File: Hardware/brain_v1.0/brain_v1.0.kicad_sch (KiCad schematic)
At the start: 50 parts, among them J1 UART, J2 Conn_01x02, J3 Conn_01x02, J4 Conn_01x02, J5 JTAG, J6 Conn_01x02, J9 UART Backup, Q1 BSS138, Q2 BSS138, Q3 BSS138, Q4 BSS138, Q5 SMD-TRANSISTORS-NPN-25V-500MW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, Q6 SMD-TRANSISTORS-NPN-25V-500MW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, SW1 SW_Push, SW3 SW_Push, U1 ESP32-WROOM-32E 4MB

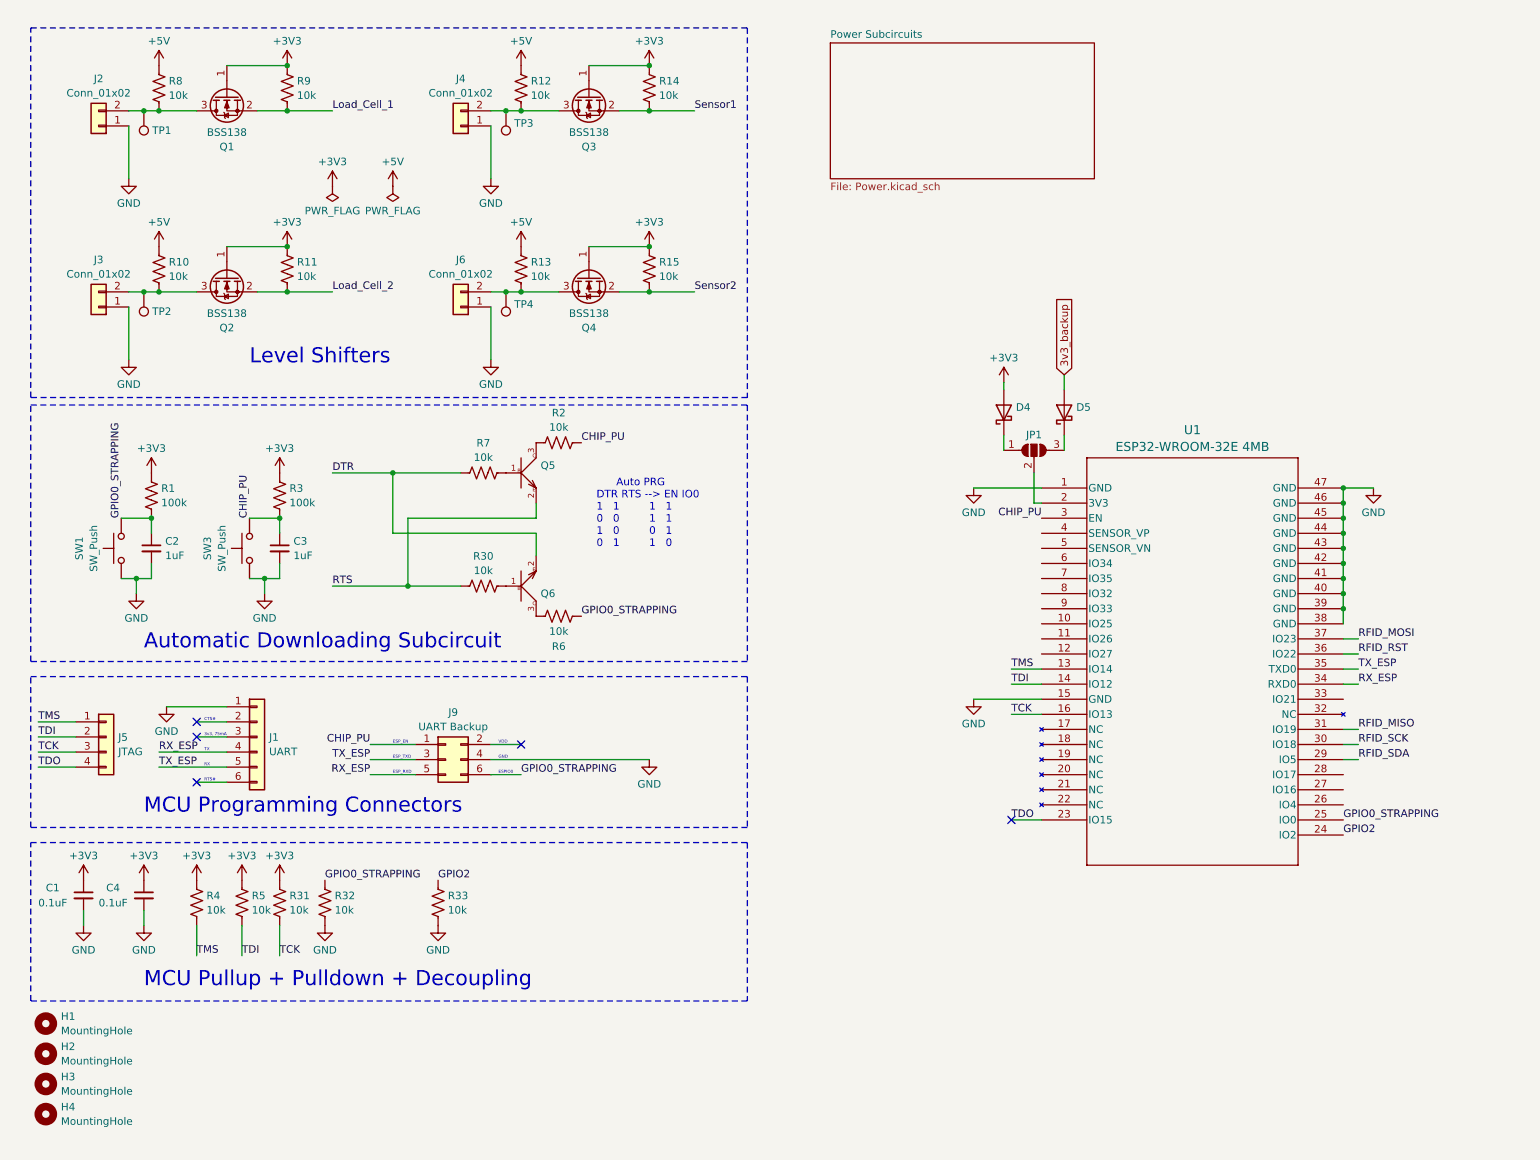
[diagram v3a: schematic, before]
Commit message: everything done on design and parts for first board run except for ADC; onto layout
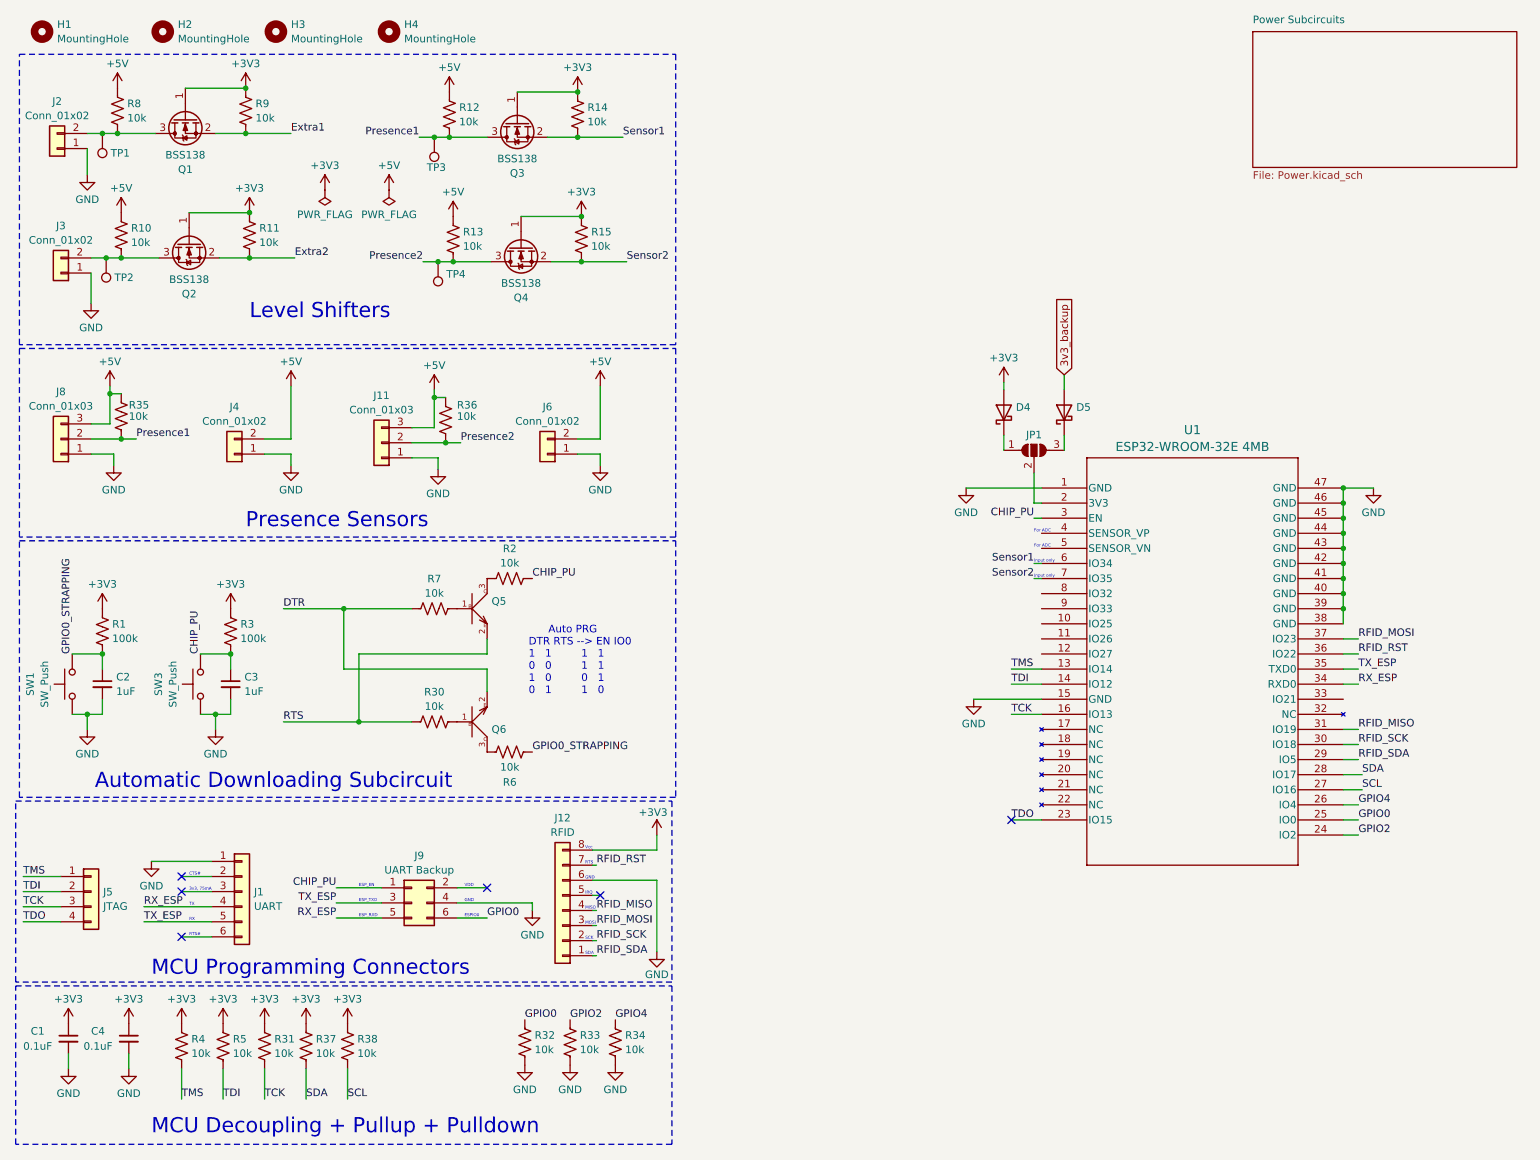
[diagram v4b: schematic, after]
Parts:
- added J11, J8: Conn_01x03, Connector_Molex:Molex_KK-254_AE-6410-03A_1x03_P2.54mm_Vertical, symbol Connector_Generic:Conn_01x03
- added J12: RFID, Connector_Harting:Harting_har-flexicon_14110813001xxx_1x08-MP_P2.54mm_Vertical, symbol Connector_Generic:Conn_01x08
- added R34, R35, R36, R37, R38: 10k, Resistor_SMD:R_1206_3216Metric, symbol Device:R_US
- J1: footprint (none) -> Connector_PinHeader_2.54mm:PinHeader_1x06_P2.54mm_Vertical; Link (none) -> https://www.digikey.com/en/products/detail/harwin-inc/M20-9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; MPN (none) -> M20-9990645
- J5: footprint (none) -> Connector_PinSocket_2.54mm:PinSocket_1x04_P2.54mm_Vertical; Link (none) -> https://www.digikey.com/en/products/detail/harwin-inc/M20-9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; MPN (none) -> M20-9990446
- J9: footprint (none) -> 61200621621:61200621621; Link (none) -> https://www.digikey.com/en/products/detail/w%C3%BCrth-elekt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; MPN (none) -> 61200621621
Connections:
- net +3V3: now also J12.8 (Pin_8), R37.1, R38.1
- net +5V: now also J4.2 (Pin_2), J6.2 (Pin_2), J11.3 (Pin_3), J8.3 (Pin_3), R35.1, R36.1
- net GND: now also J11.1 (Pin_1), J12.6 (Pin_6), J8.1 (Pin_1), R34.2
- net GPIO0_STRAPPING: no longer J9.6 (Pin_6), R32.1, U1.25 (IO0)
- net RFID_MISO: now also J12.4 (Pin_4)
- net RFID_MOSI: now also J12.3 (Pin_3)
- net RFID_RST: now also J12.7 (Pin_7)
- net RFID_SCK: now also J12.2 (Pin_2)
- net RFID_SDA: now also J12.1 (Pin_1)
- net Sensor1: now also U1.6 (IO34)
- net Sensor2: now also U1.7 (IO35)
- net Presence2: now reaches Q4.3 (D), R13.2, TP4.1
- net Presence2: now also J11.2 (Pin_2), R36.2; no longer J6.2 (Pin_2)
- net Presence1: now reaches Q3.3 (D), R12.2, TP3.1
- net Presence1: now also J8.2 (Pin_2), R35.2; no longer J4.2 (Pin_2)
- net GPIO4: now reaches U1.26 (IO4)
- net GPIO4: now also R34.1
- net SCL: now reaches U1.27 (IO16)
- net SCL: now also R38.2
- net SDA: now reaches U1.28 (IO17)
- net SDA: now also R37.2
- net Load_Cell_1 renamed Extra1
- net Load_Cell_2 renamed Extra2
- new net GPIO0: J9.6 (Pin_6), R32.1, U1.25 (IO0)
- no-connect marks 5 -> 6
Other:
- note added: "For ADC"
- note added: "IRQ"
- note added: "Input only"
- note added: "MCU Decoupling + Pullup + Pulldown"
- note added: "MISO"
- note added: "MOSI"
- note added: "Presence Sensors"
- note added: "RTS"
- note added: "SCK"
- note added: "SDA"
- note added: "Vcc"
- note removed: "MCU Pullup + Pulldown + Decoupling"
- moved on the sheet: C1, C2, C3, C4, H1, H2, H3, H4, J1, J2, J3, J4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

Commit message: finished part selection and schematic for brain. Created RFID and Motor Driver boards
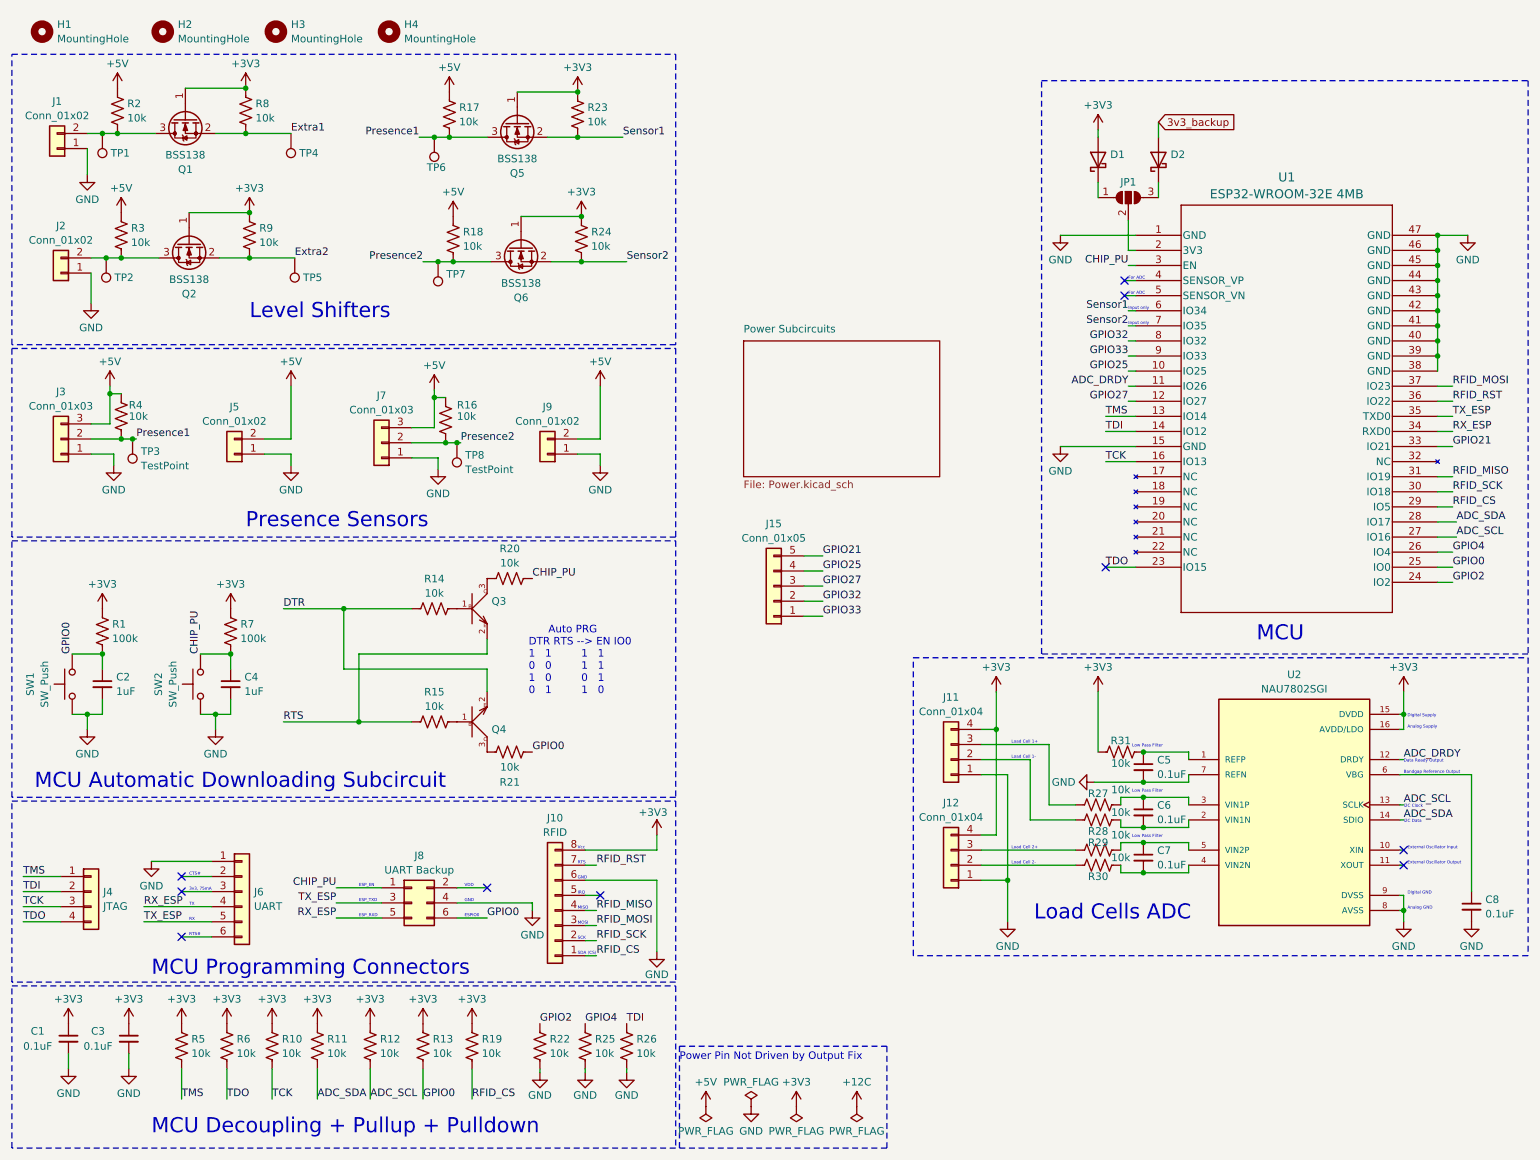
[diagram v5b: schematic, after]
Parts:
- removed R34: 10k, Resistor_SMD:R_1206_3216Metric, symbol Device:R_US
- added C5, C6, C7, C8: 0.1uF, Capacitor_SMD:C_0603_1608Metric, symbol Device:C_Small
- added J11, J12: Conn_01x04, Connector_Molex:Molex_KK-254_AE-6410-04A_1x04_P2.54mm_Vertical, symbol Connector_Generic:Conn_01x04
- added J15: Conn_01x05, symbol Connector_Generic:Conn_01x05
- added R13, R19, R26, R27, R28, R29, R30, R31: 10k, Resistor_SMD:R_1206_3216Metric, symbol Device:R_US
- added TP3, TP4, TP5, TP8: TestPoint, TestPoint:TestPoint_Keystone_5010-5014_Multipurpose, symbol Connector:TestPoint
- added U2: NAU7802SGI, NAU7802SGI:SOIC127P600X175-16N, symbol NAU7802SGI:NAU7802SGI
- renumbered C4 to C3, C3 to C4, D4 to D1, D5 to D2, J2 to J1, J12 to J10, J3 to J2, J8 to J3, J5 to J4, J4 to J5, J1 to J6, J11 to J7, J9 to J8, J6 to J9, Q5 to Q3, Q6 to Q4, Q3 to Q5, Q4 to Q6, R31 to R10, R37 to R11, R38 to R12, R7 to R14, R30 to R15, R36 to R16, R12 to R17, R13 to R18, R8 to R2, R2 to R20, R6 to R21, R32 to R22, R14 to R23, R15 to R24, R33 to R25, R10 to R3, R35 to R4, R4 to R5, R5 to R6, R3 to R7, R9 to R8, R11 to R9, SW3 to SW2, TP3 to TP6, TP4 to TP7
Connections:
- net GPIO0_STRAPPING is gone; now on net GPIO0: C2.1, R1.2, R21.2, SW1.2
- net +3V3: now also J11.4 (Pin_4), J12.4 (Pin_4), R13.1, R19.1, R31.1, U2.15 (DVDD), U2.16 (AVDD/LDO)
- net Extra1: now also TP4.1
- net Extra2: now also TP5.1
- net GND: now also C5.2, C8.2, J11.1 (Pin_1), J12.1 (Pin_1), R26.2, U2.7 (REFN), U2.8 (AVSS), U2.9 (DVSS)
- net GPIO0: now also R13.2; no longer R22.1
- net GPIO2: now also R22.1; no longer R25.1
- net GPIO4: now also R25.1
- net Presence1: now also TP3.1
- net Presence2: now also TP8.1
- net TDI: now also R26.1; no longer R6.2
- net TDO: now also R6.2
- net GPIO25: now reaches U1.10 (IO25)
- net GPIO25: now also J15.4 (Pin_4)
- net ADC_DRDY: now reaches U1.11 (IO26)
- net ADC_DRDY: now also U2.12 (DRDY)
- net GPIO27: now reaches U1.12 (IO27)
- net GPIO27: now also J15.3 (Pin_3)
- net GPIO21: now reaches U1.33 (IO21)
- net GPIO21: now also J15.5 (Pin_5)
- net GPIO32: now reaches U1.8 (IO32)
- net GPIO32: now also J15.2 (Pin_2)
- net GPIO33: now reaches U1.9 (IO33)
- net GPIO33: now also J15.1 (Pin_1)
- net RFID_SDA renamed RFID_CS
- net RFID_CS: now also R19.2
- net SCL renamed ADC_SCL
- net ADC_SCL: now also U2.13 (SCLK)
- net SDA renamed ADC_SDA
- net ADC_SDA: now also U2.14 (SDIO)
- new net: C5.1, R31.2, U2.1 (REFP)
- new net: C6.1, R27.2, U2.3 (VIN1P)
- new net: C6.2, R28.2, U2.2 (VIN1N)
- new net: C7.1, R29.2, U2.5 (VIN2P)
- new net: C7.2, R30.2, U2.4 (VIN2N)
- new net: C8.1, U2.6 (VBG)
- new net: J12.2 (Pin_2), R30.1
- new net: J11.2 (Pin_2), R28.1
- new net: J11.3 (Pin_3), R27.1
- new net: J12.3 (Pin_3), R29.1
- no-connect marks 6 -> 10
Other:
- note added: "Analog GND"
- note added: "Analog Supply"
- note added: "Bandgap Reference Output"
- note added: "Data Ready Output"
- note added: "Digital GND"
- note added: "Digital Supply"
- note added: "External Oscillator Input"
- note added: "External Oscillator Output"
- note added: "I2C Clock"
- note added: "I2C Data"
- note added: "Load Cell 1+"
- note added: "Load Cell 1-"
- note added: "Load Cell 2+"
- note added: "Load Cell 2-"
- note added: "Load Cells ADC"
- note added: "Low Pass Filter"
- note added: "MCU"
- note added: "MCU Automatic Downloading Subcircuit"
- note added: "Power Pin Not Driven by Output Fix"
- note added: "SDA (CS)"
- note removed: "Automatic Downloading Subcircuit"
- note removed: "SDA"
- moved on the sheet: D1, D2, J10, JP1, R10, R11, R12, R22, R25, R6, U1

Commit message: RFID board schematic done, antenna head created in the layout
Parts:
- J15: footprint (none) -> Connector_PinHeader_2.54mm:PinHeader_1x05_P2.54mm_Vertical; Link (none) -> https://www.digikey.com/en/products/detail/harwin-inc/M20-9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; MPN (none) -> M20-9990546
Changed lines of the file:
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@@
       (effects (font (size 1.27 1.27)))
     )
-    (property "Footprint" "" (at 140.335 109.22 0)
+    (property "Footprint" "Connector_PinHeader_2.54mm:PinHeader_1x05_P2.54mm_Vertical" (at 140.335 109.22 0)
       (effects (font (size 1.27 1.27)) hide)
     )
@@
       (effects (font (size 1.27 1.27)) hide)
     )
+    (property "Link" "https://www.digikey.com/en/products/detail/harwin-inc/M20-9990546/3728232" (at 140.335 109.22 0)
+      (effects (font (size 1.27 1.27)) hide)
+    )
+    (property "MPN" "M20-9990546" (at 140.335 109.22 0)
+      (effects (font (size 1.27 1.27)) hide)
+    )
